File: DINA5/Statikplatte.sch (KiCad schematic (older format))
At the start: 31 parts, among them J1 VIN, J10 HV, J2 GND, J3 GND, J4 GND, J5 GND, J6 GND, J7 HV, J8 HV, J9 HV

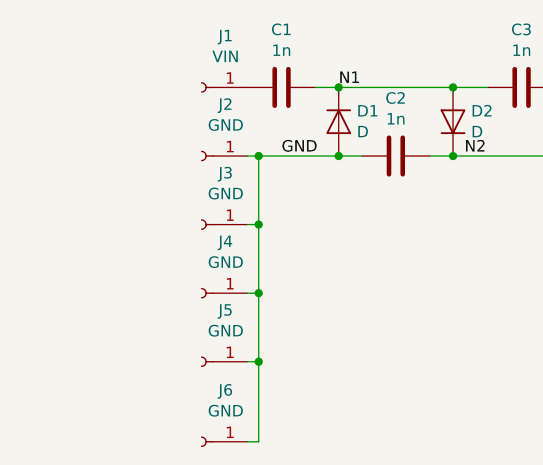
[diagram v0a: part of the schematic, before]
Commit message: added screws
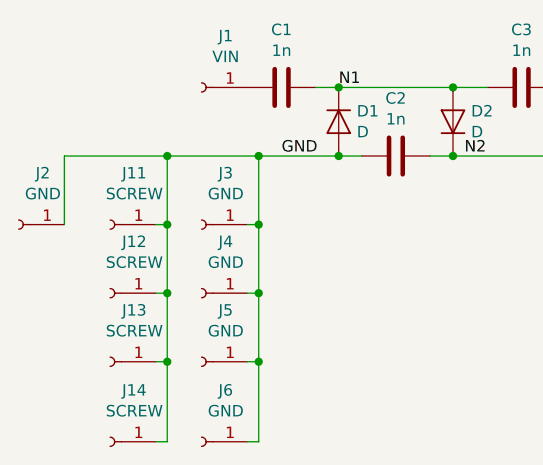
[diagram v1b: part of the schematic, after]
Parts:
- added J11, J12, J13, J14: SCREW, otter:M3_Screw, symbol Connector:Conn_01x01_Female
- J10, J2, J4, J5, J6, J7, J8, J9: footprint TestPoint:TestPoint_Pad_2.5x2.5mm -> otter:PAD7.5x12
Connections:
- net GND: now also J11.1 (Pin_1), J12.1 (Pin_1), J13.1 (Pin_1), J14.1 (Pin_1)
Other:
- moved on the sheet: J2
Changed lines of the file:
@@
 EESchema Schematic File Version 4
+LIBS:Statikplatte-cache
 EELAYER 26 0
 EELAYER END
@@
 L Connector:Conn_01x01_Female J2
 U 1 1 5C48BB48
-P 3850 3750
-F 0 "J2" H 3744 3525 50  0000 C CNN
-F 1 "GND" H 3744 3616 50  0000 C CNN
-F 2 "TestPoint:TestPoint_Pad_2.5x2.5mm" H 3850 3750 50  0001 C CNN
-F 3 "~" H 3850 3750 50  0001 C CNN
-	1    3850 3750
+P 3050 4050
+F 0 "J2" H 2944 3825 50  0000 C CNN
+F 1 "GND" H 2944 3916 50  0000 C CNN
+F 2 "otter:PAD7.5x12" H 3050 4050 50  0001 C CNN
+F 3 "~" H 3050 4050 50  0001 C CNN
+	1    3050 4050
 	-1   0    0    1
 $EndComp
@@
 F 0 "J8" H 10078 3976 50  0000 L CNN
 F 1 "HV" H 10078 3885 50  0000 L CNN
-F 2 "TestPoint:TestPoint_Pad_2.5x2.5mm" H 10050 3950 50  0001 C CNN
+F 2 "otter:PAD7.5x12" H 10050 3950 50  0001 C CNN
 F 3 "~" H 10050 3950 50  0001 C CNN
 	1    10050 3950
@@
 F 0 "J7" H 10078 3776 50  0000 L CNN
 F 1 "HV" H 10078 3685 50  0000 L CNN
-F 2 "TestPoint:TestPoint_Pad_2.5x2.5mm" H 10050 3750 50  0001 C CNN
+F 2 "otter:PAD7.5x12" H 10050 3750 50  0001 C CNN
 F 3 "~" H 10050 3750 50  0001 C CNN
 	1    10050 3750
@@
 F 0 "J9" H 10078 4176 50  0000 L CNN
 F 1 "HV" H 10078 4085 50  0000 L CNN
-F 2 "TestPoint:TestPoint_Pad_2.5x2.5mm" H 10050 4150 50  0001 C CNN
+F 2 "otter:PAD7.5x12" H 10050 4150 50  0001 C CNN
 F 3 "~" H 10050 4150 50  0001 C CNN
 	1    10050 4150
@@
 F 0 "J10" H 10078 4376 50  0000 L CNN
 F 1 "HV" H 10078 4285 50  0000 L CNN
-F 2 "TestPoint:TestPoint_Pad_2.5x2.5mm" H 10050 4350 50  0001 C CNN
+F 2 "otter:PAD7.5x12" H 10050 4350 50  0001 C CNN
 F 3 "~" H 10050 4350 50  0001 C CNN
 	1    10050 4350
@@
 F 0 "J4" H 3744 4125 50  0000 C CNN
 F 1 "GND" H 3744 4216 50  0000 C CNN
-F 2 "TestPoint:TestPoint_Pad_2.5x2.5mm" H 3850 4350 50  0001 C CNN
+F 2 "otter:PAD7.5x12" H 3850 4350 50  0001 C CNN
 F 3 "~" H 3850 4350 50  0001 C CNN
 	1    3850 4350
@@
 F 0 "J5" H 3744 4425 50  0000 C CNN
 F 1 "GND" H 3744 4516 50  0000 C CNN
-F 2 "TestPoint:TestPoint_Pad_2.5x2.5mm" H 3850 4650 50  0001 C CNN
+F 2 "otter:PAD7.5x12" H 3850 4650 50  0001 C CNN
 F 3 "~" H 3850 4650 50  0001 C CNN
 	1    3850 4650
@@
 F 0 "J6" H 3744 4775 50  0000 C CNN
 F 1 "GND" H 3744 4866 50  0000 C CNN
-F 2 "TestPoint:TestPoint_Pad_2.5x2.5mm" H 3850 5000 50  0001 C CNN
+F 2 "otter:PAD7.5x12" H 3850 5000 50  0001 C CNN
 F 3 "~" H 3850 5000 50  0001 C CNN
 	1    3850 5000
@@
 $EndComp
 Connection ~ 4100 3750
-Wire Wire Line
-	4100 3750 4050 3750
 Wire Wire Line
 	4050 5000 4100 5000
@@
 Text Label 9650 3750 0    50   ~ 0
 HV
+$Comp
+L Connector:Conn_01x01_Female J11
+U 1 1 5C61C794
+P 3450 4050
+F 0 "J11" H 3344 3825 50  0000 C CNN
+F 1 "SCREW" H 3344 3916 50  0000 C CNN
+F 2 "otter:M3_Screw" H 3450 4050 50  0001 C CNN
+F 3 "~" H 3450 4050 50  0001 C CNN
+	1    3450 4050
+	-1   0    0    1
+$EndComp
+$Comp
+L Connector:Conn_01x01_Female J12
+U 1 1 5C61E45B
+P 3450 4350
+F 0 "J12" H 3344 4125 50  0000 C CNN
+F 1 "SCREW" H 3344 4216 50  0000 C CNN
+F 2 "otter:M3_Screw" H 3450 4350 50  0001 C CNN
+F 3 "~" H 3450 4350 50  0001 C CNN
+	1    3450 4350
+	-1   0    0    1
+$EndComp
+$Comp
+L Connector:Conn_01x01_Female J13
+U 1 1 5C61F06D
+P 3450 4650
+F 0 "J13" H 3344 4425 50  0000 C CNN
+F 1 "SCREW" H 3344 4516 50  0000 C CNN
+F 2 "otter:M3_Screw" H 3450 4650 50  0001 C CNN
+F 3 "~" H 3450 4650 50  0001 C CNN
+	1    3450 4650
+	-1   0    0    1
+$EndComp
+$Comp
+L Connector:Conn_01x01_Female J14
+U 1 1 5C61FC91
+P 3450 5000
+F 0 "J14" H 3344 4775 50  0000 C CNN
+F 1 "SCREW" H 3344 4866 50  0000 C CNN
+F 2 "otter:M3_Screw" H 3450 5000 50  0001 C CNN
+F 3 "~" H 3450 5000 50  0001 C CNN
+	1    3450 5000
+	-1   0    0    1
+$EndComp
+Wire Wire Line
+	3250 4050 3250 3750
+Wire Wire Line
+	3250 3750 3700 3750
+Wire Wire Line
+	3650 5000 3700 5000
+Wire Wire Line
+	3700 5000 3700 4650
+Connection ~ 3700 3750
+Wire Wire Line
+	3700 3750 4100 3750
+Wire Wire Line
+	3650 4050 3700 4050
+Connection ~ 3700 4050
+Wire Wire Line
+	3700 4050 3700 3750
+Wire Wire Line
+	3650 4350 3700 4350
+Connection ~ 3700 4350
+Wire Wire Line
+	3700 4350 3700 4050
+Wire Wire Line
+	3650 4650 3700 4650
+Connection ~ 3700 4650
+Wire Wire Line
+	3700 4650 3700 4350
 $EndSCHEMATC

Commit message: added resistor to gnd
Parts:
- added R2: 33M, Resistor_SMD:R_2512_6332Metric, symbol Device:R
- J11, J12, J13, J14: symbol Connector:Conn_01x01_Female -> Connector:Conn_01x02_Female
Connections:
- net GND: now also R2.2; no longer J11.1 (Pin_1), J12.1 (Pin_1), J13.1 (Pin_1), J14.1 (Pin_1), J2.1 (Pin_1), J4.1 (Pin_1), J5.1 (Pin_1), J6.1 (Pin_1)
- new net GNDE: J11.1 (Pin_1), J11.2 (Pin_2), J12.1 (Pin_1), J12.2 (Pin_2), J13.1 (Pin_1), J13.2 (Pin_2), J14.1 (Pin_1), J14.2 (Pin_2), J2.1 (Pin_1), J4.1 (Pin_1), J5.1 (Pin_1), J6.1 (Pin_1), R2.1
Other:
- moved on the sheet: J2, J3, J4, J5, J6
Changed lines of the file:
@@
 	4550 3750 4450 3750
 Connection ~ 4450 3750
-Wire Wire Line
-	4450 3750 4100 3750
 $Comp
 L Device:C C3
@@
 L Connector:Conn_01x01_Female J2
 U 1 1 5C48BB48
-P 3050 4050
-F 0 "J2" H 2944 3825 50  0000 C CNN
-F 1 "GND" H 2944 3916 50  0000 C CNN
-F 2 "otter:PAD7.5x12" H 3050 4050 50  0001 C CNN
-F 3 "~" H 3050 4050 50  0001 C CNN
-	1    3050 4050
+P 4300 4500
+F 0 "J2" H 4194 4275 50  0000 C CNN
+F 1 "GND" H 4194 4366 50  0000 C CNN
+F 2 "otter:PAD7.5x12" H 4300 4500 50  0001 C CNN
+F 3 "~" H 4300 4500 50  0001 C CNN
+	1    4300 4500
 	-1   0    0    1
 $EndComp
@@
 L Connector:Conn_01x01_Female J3
 U 1 1 5C48FB05
-P 3850 4050
-F 0 "J3" H 3744 3825 50  0000 C CNN
-F 1 "GND" H 3744 3916 50  0000 C CNN
-F 2 "TestPoint:TestPoint_Pad_2.5x2.5mm" H 3850 4050 50  0001 C CNN
-F 3 "~" H 3850 4050 50  0001 C CNN
-	1    3850 4050
+P 3850 3750
+F 0 "J3" H 3744 3525 50  0000 C CNN
+F 1 "GND" H 3744 3616 50  0000 C CNN
+F 2 "TestPoint:TestPoint_Pad_2.5x2.5mm" H 3850 3750 50  0001 C CNN
+F 3 "~" H 3850 3750 50  0001 C CNN
+	1    3850 3750
 	-1   0    0    1
 $EndComp
@@
 L Connector:Conn_01x01_Female J4
 U 1 1 5C490265
-P 3850 4350
-F 0 "J4" H 3744 4125 50  0000 C CNN
-F 1 "GND" H 3744 4216 50  0000 C CNN
-F 2 "otter:PAD7.5x12" H 3850 4350 50  0001 C CNN
-F 3 "~" H 3850 4350 50  0001 C CNN
-	1    3850 4350
+P 4300 4800
+F 0 "J4" H 4194 4575 50  0000 C CNN
+F 1 "GND" H 4194 4666 50  0000 C CNN
+F 2 "otter:PAD7.5x12" H 4300 4800 50  0001 C CNN
+F 3 "~" H 4300 4800 50  0001 C CNN
+	1    4300 4800
 	-1   0    0    1
 $EndComp
@@
 L Connector:Conn_01x01_Female J5
 U 1 1 5C490A61
-P 3850 4650
-F 0 "J5" H 3744 4425 50  0000 C CNN
-F 1 "GND" H 3744 4516 50  0000 C CNN
-F 2 "otter:PAD7.5x12" H 3850 4650 50  0001 C CNN
-F 3 "~" H 3850 4650 50  0001 C CNN
-	1    3850 4650
+P 4300 5100
+F 0 "J5" H 4194 4875 50  0000 C CNN
+F 1 "GND" H 4194 4966 50  0000 C CNN
+F 2 "otter:PAD7.5x12" H 4300 5100 50  0001 C CNN
+F 3 "~" H 4300 5100 50  0001 C CNN
+	1    4300 5100
 	-1   0    0    1
 $EndComp
@@
 L Connector:Conn_01x01_Female J6
 U 1 1 5C4911D9
-P 3850 5000
-F 0 "J6" H 3744 4775 50  0000 C CNN
-F 1 "GND" H 3744 4866 50  0000 C CNN
-F 2 "otter:PAD7.5x12" H 3850 5000 50  0001 C CNN
-F 3 "~" H 3850 5000 50  0001 C CNN
-	1    3850 5000
-	-1   0    0    1
-$EndComp
-Connection ~ 4100 3750
-Wire Wire Line
-	4050 5000 4100 5000
-Wire Wire Line
-	4100 3750 4100 4050
-Wire Wire Line
-	4100 4050 4050 4050
-Connection ~ 4100 4050
-Wire Wire Line
-	4100 4050 4100 4350
-Wire Wire Line
-	4050 4350 4100 4350
-Connection ~ 4100 4350
-Wire Wire Line
-	4100 4350 4100 4650
-Wire Wire Line
-	4050 4650 4100 4650
-Connection ~ 4100 4650
-Wire Wire Line
-	4100 4650 4100 5000
+P 4300 5450
+F 0 "J6" H 4194 5225 50  0000 C CNN
+F 1 "GND" H 4194 5316 50  0000 C CNN
+F 2 "otter:PAD7.5x12" H 4300 5450 50  0001 C CNN
+F 3 "~" H 4300 5450 50  0001 C CNN
+	1    4300 5450
+	-1   0    0    1
+$EndComp
+Wire Wire Line
+	4500 5450 4550 5450
+Wire Wire Line
+	4550 4200 4550 4500
+Wire Wire Line
+	4550 4500 4500 4500
+Connection ~ 4550 4500
+Wire Wire Line
+	4550 4500 4550 4800
+Wire Wire Line
+	4500 4800 4550 4800
+Connection ~ 4550 4800
+Wire Wire Line
+	4550 4800 4550 5100
+Wire Wire Line
+	4500 5100 4550 5100
+Connection ~ 4550 5100
+Wire Wire Line
+	4550 5100 4550 5450
 Text Label 4200 3750 0    50   ~ 0
 GND
@@
 Text Label 9650 3750 0    50   ~ 0
 HV
-$Comp
-L Connector:Conn_01x01_Female J11
+Wire Wire Line
+	4100 5450 4150 5450
+Wire Wire Line
+	4150 5450 4150 5350
+Wire Wire Line
+	4100 4500 4150 4500
+Connection ~ 4150 4500
+Wire Wire Line
+	4100 4800 4150 4800
+Connection ~ 4150 4800
+Wire Wire Line
+	4150 4800 4150 4700
+Wire Wire Line
+	4100 5100 4150 5100
+Connection ~ 4150 5100
+Wire Wire Line
+	4150 5100 4150 5000
+$Comp
+L Device:R R2
+U 1 1 5C632141
+P 4150 3950
+F 0 "R2" V 3943 3950 50  0000 C CNN
+F 1 "33M" V 4034 3950 50  0000 C CNN
+F 2 "Resistor_SMD:R_2512_6332Metric" V 4080 3950 50  0001 C CNN
+F 3 "~" H 4150 3950 50  0001 C CNN
+	1    4150 3950
+	-1   0    0    1
+$EndComp
+Wire Wire Line
+	4150 4100 4150 4200
+Wire Wire Line
+	4550 4200 4150 4200
+Connection ~ 4150 4200
+Wire Wire Line
+	4150 4200 4150 4400
+Wire Wire Line
+	4050 3750 4150 3750
+Wire Wire Line
+	4150 3800 4150 3750
+Connection ~ 4150 3750
+Wire Wire Line
+	4150 3750 4450 3750
+Text Label 4250 4200 0    50   ~ 0
+GNDE
+$Comp
+L Connector:Conn_01x02_Female J14
+U 1 1 5C61FC91
+P 3900 5450
+F 0 "J14" H 3794 5225 50  0000 C CNN
+F 1 "SCREW" H 3794 5316 50  0000 C CNN
+F 2 "otter:M3_Screw" H 3900 5450 50  0001 C CNN
+F 3 "~" H 3900 5450 50  0001 C CNN
+	1    3900 5450
+	-1   0    0    1
+$EndComp
+$Comp
+L Connector:Conn_01x02_Female J13
+U 1 1 5C61F06D
+P 3900 5100
+F 0 "J13" H 3794 4875 50  0000 C CNN
+F 1 "SCREW" H 3794 4966 50  0000 C CNN
+F 2 "otter:M3_Screw" H 3900 5100 50  0001 C CNN
+F 3 "~" H 3900 5100 50  0001 C CNN
+	1    3900 5100
+	-1   0    0    1
+$EndComp
+$Comp
+L Connector:Conn_01x02_Female J12
+U 1 1 5C61E45B
+P 3900 4800
+F 0 "J12" H 3794 4575 50  0000 C CNN
+F 1 "SCREW" H 3794 4666 50  0000 C CNN
+F 2 "otter:M3_Screw" H 3900 4800 50  0001 C CNN
+F 3 "~" H 3900 4800 50  0001 C CNN
+	1    3900 4800
+	-1   0    0    1
+$EndComp
+$Comp
+L Connector:Conn_01x02_Female J11
 U 1 1 5C61C794
-P 3450 4050
-F 0 "J11" H 3344 3825 50  0000 C CNN
-F 1 "SCREW" H 3344 3916 50  0000 C CNN
-F 2 "otter:M3_Screw" H 3450 4050 50  0001 C CNN
-F 3 "~" H 3450 4050 50  0001 C CNN
-	1    3450 4050
-	-1   0    0    1
-$EndComp
-$Comp
-L Connector:Conn_01x01_Female J12
-U 1 1 5C61E45B
-P 3450 4350
-F 0 "J12" H 3344 4125 50  0000 C CNN
-F 1 "SCREW" H 3344 4216 50  0000 C CNN
-F 2 "otter:M3_Screw" H 3450 4350 50  0001 C CNN
-F 3 "~" H 3450 4350 50  0001 C CNN
-	1    3450 4350
-	-1   0    0    1
-$EndComp
-$Comp
-L Connector:Conn_01x01_Female J13
-U 1 1 5C61F06D
-P 3450 4650
-F 0 "J13" H 3344 4425 50  0000 C CNN
-F 1 "SCREW" H 3344 4516 50  0000 C CNN
-F 2 "otter:M3_Screw" H 3450 4650 50  0001 C CNN
-F 3 "~" H 3450 4650 50  0001 C CNN
-	1    3450 4650
-	-1   0    0    1
-$EndComp
-$Comp
-L Connector:Conn_01x01_Female J14
-U 1 1 5C61FC91
-P 3450 5000
-F 0 "J14" H 3344 4775 50  0000 C CNN
-F 1 "SCREW" H 3344 4866 50  0000 C CNN
-F 2 "otter:M3_Screw" H 3450 5000 50  0001 C CNN
-F 3 "~" H 3450 5000 50  0001 C CNN
-	1    3450 5000
-	-1   0    0    1
-$EndComp
-Wire Wire Line
-	3250 4050 3250 3750
-Wire Wire Line
-	3250 3750 3700 3750
-Wire Wire Line
-	3650 5000 3700 5000
-Wire Wire Line
-	3700 5000 3700 4650
-Connection ~ 3700 3750
-Wire Wire Line
-	3700 3750 4100 3750
-Wire Wire Line
-	3650 4050 3700 4050
-Connection ~ 3700 4050
-Wire Wire Line
-	3700 4050 3700 3750
-Wire Wire Line
-	3650 4350 3700 4350
-Connection ~ 3700 4350
-Wire Wire Line
-	3700 4350 3700 4050
-Wire Wire Line
-	3650 4650 3700 4650
-Connection ~ 3700 4650
-Wire Wire Line
-	3700 4650 3700 4350
+P 3900 4500
+F 0 "J11" H 3794 4275 50  0000 C CNN
+F 1 "SCREW" H 3794 4366 50  0000 C CNN
+F 2 "otter:M3_Screw" H 3900 4500 50  0001 C CNN
+F 3 "~" H 3900 4500 50  0001 C CNN
+	1    3900 4500
+	-1   0    0    1
+$EndComp
+Wire Wire Line
+	4100 5350 4150 5350
+Connection ~ 4150 5350
+Wire Wire Line
+	4150 5350 4150 5100
+Wire Wire Line
+	4100 4700 4150 4700
+Connection ~ 4150 4700
+Wire Wire Line
+	4150 4700 4150 4500
+Wire Wire Line
+	4100 5000 4150 5000
+Connection ~ 4150 5000
+Wire Wire Line
+	4150 5000 4150 4800
+Wire Wire Line
+	4100 4400 4150 4400
+Connection ~ 4150 4400
+Wire Wire Line
+	4150 4400 4150 4500
 $EndSCHEMATC

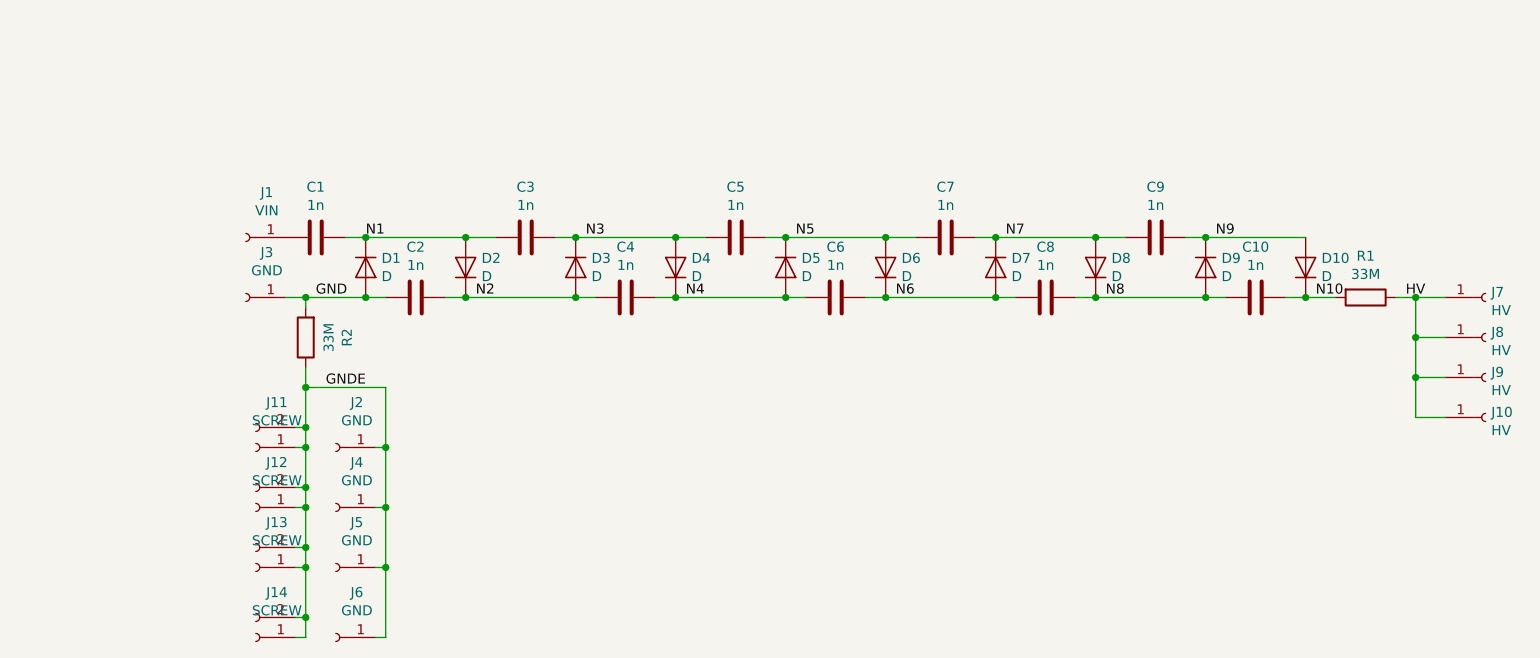
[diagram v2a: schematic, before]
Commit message: added negative kaskade
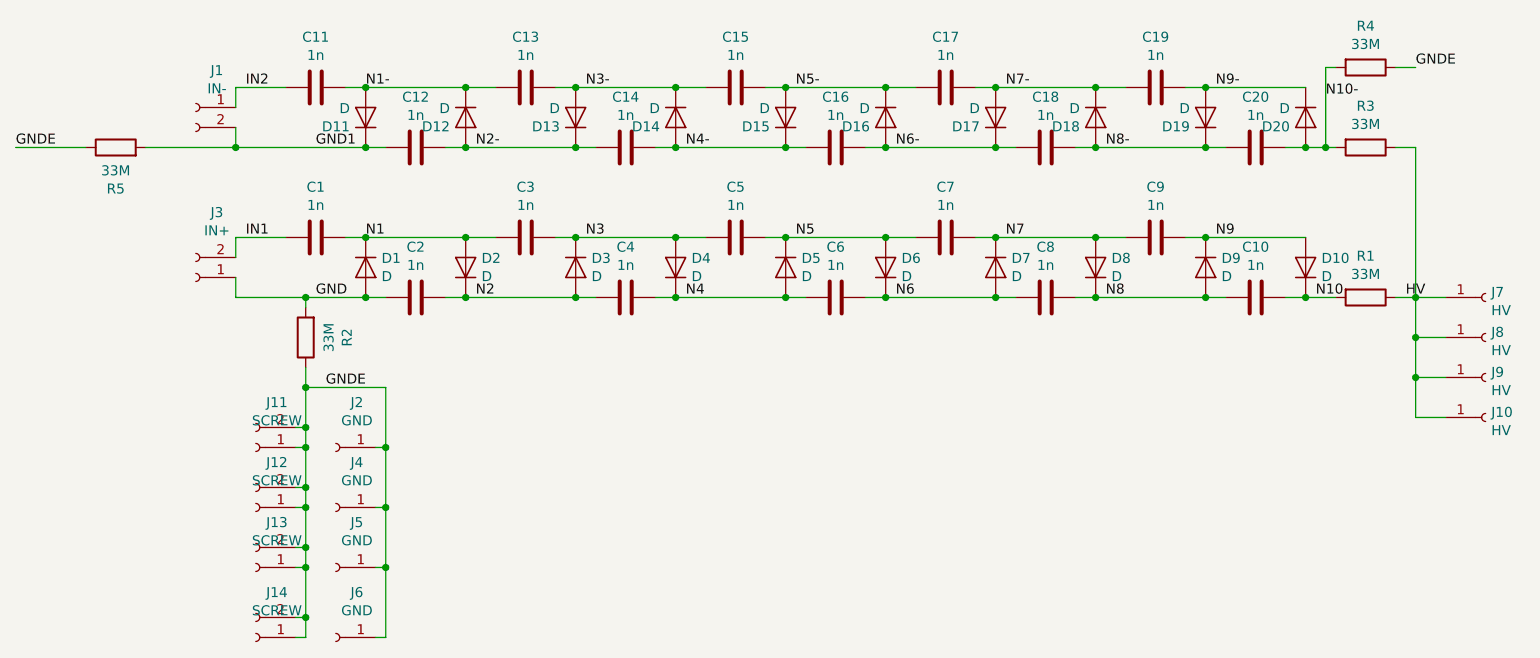
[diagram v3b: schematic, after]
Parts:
- removed J1: VIN, TestPoint:TestPoint_Pad_2.5x2.5mm, symbol Connector:Conn_01x01_Female
- removed J3: GND, TestPoint:TestPoint_Pad_2.5x2.5mm, symbol Connector:Conn_01x01_Female
- added C11, C12, C13, C14, C15, C16, C17, C18, C19, C20: 1n, Capacitor_SMD:C_1812_4532Metric, symbol Device:C
- added D11, D12, D13, D14, D15, D16, D17, D18, D19, D20: D, otter:SMAF, symbol Device:D
- added J1: IN-, otter:LED_Connector, symbol Connector:Conn_01x02_Female
- added J3: IN+, otter:LED_Connector, symbol Connector:Conn_01x02_Female
- added R3, R4, R5: 33M, Resistor_SMD:R_2512_6332Metric, symbol Device:R
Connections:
- net GND: now also J3.1 (Pin_1)
- net GNDE: now also R4.1, R5.1
- net HV: now also R3.1
- net IN1: now reaches C1.2
- net IN1: now also J3.2 (Pin_2)
- new net GND1: C12.2, D11.1 (K), J1.2 (Pin_2), R5.2
- new net IN2: C11.2, J1.1 (Pin_1)
- new net N1-: C11.1, C13.2, D11.2 (A), D12.1 (K)
- new net N10-: C20.1, D20.2 (A), R3.2, R4.2
- new net N2-: C12.1, C14.2, D12.2 (A), D13.1 (K)
- new net N3-: C13.1, C15.2, D13.2 (A), D14.1 (K)
- new net N4-: C14.1, C16.2, D14.2 (A), D15.1 (K)
- new net N5-: C15.1, C17.2, D15.2 (A), D16.1 (K)
- new net N6-: C16.1, C18.2, D16.2 (A), D17.1 (K)
- new net N7-: C17.1, C19.2, D17.2 (A), D18.1 (K)
- new net N8-: C18.1, C20.2, D18.2 (A), D19.1 (K)
- new net N9-: C19.1, D19.2 (A), D20.1 (K)

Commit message: went back to one voltage multiplier
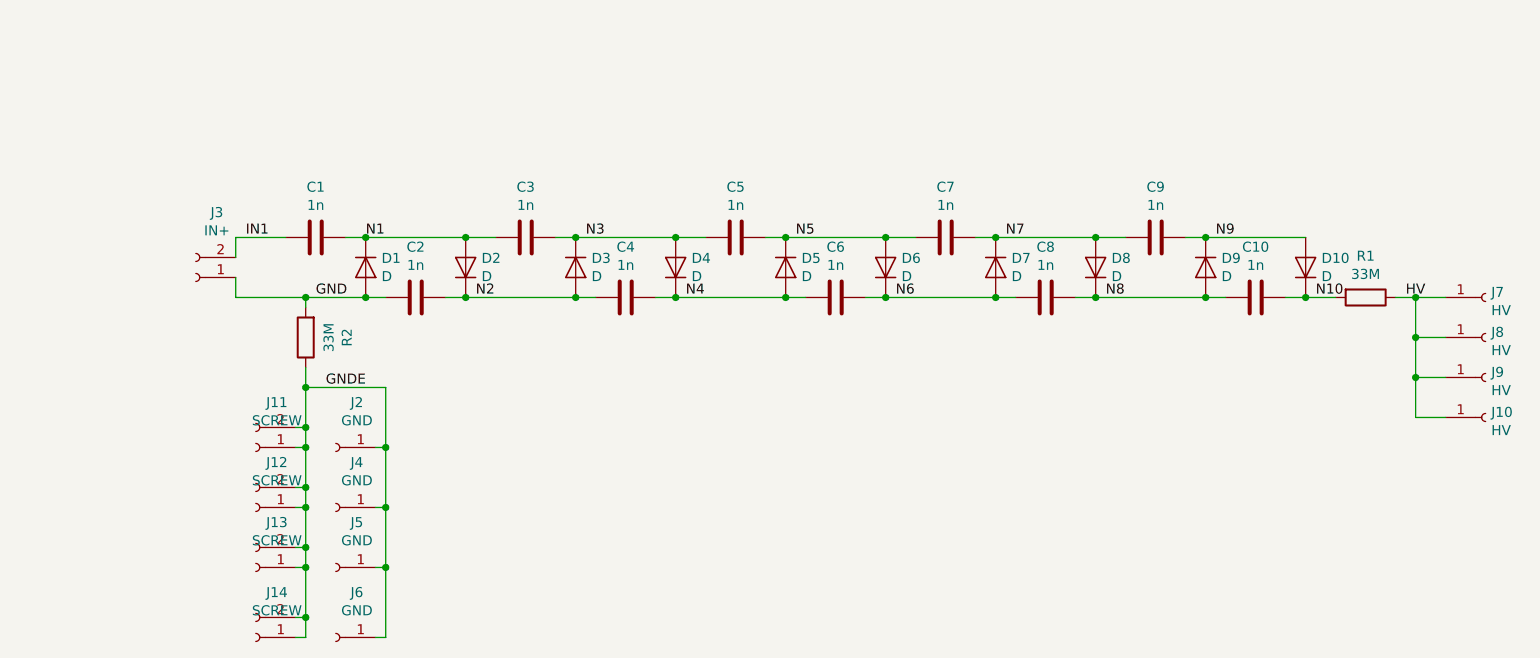
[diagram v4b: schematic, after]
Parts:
- removed C11, C12, C13, C14, C15, C16, C17, C18, C19, C20: 1n, Capacitor_SMD:C_1812_4532Metric, symbol Device:C
- removed D11, D12, D13, D14, D15, D16, D17, D18, D19, D20: D, otter:SMAF, symbol Device:D
- removed J1: IN-, otter:LED_Connector, symbol Connector:Conn_01x02_Female
- removed R3, R4, R5: 33M, Resistor_SMD:R_2512_6332Metric, symbol Device:R
